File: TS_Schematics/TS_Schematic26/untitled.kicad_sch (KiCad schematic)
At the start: 28 parts, among them K2 IR(-) - TE Connectivity, K3 IR(+) - G2RL-1, K4 Precharge_G2RL-2, SW1 RL00801-500R, SW2 RL00801-500R, SW3 RL00801-500R, SW4 RL00801-500R, SW5 RL00801-500R, SW6 RL00801-500R, SW7 RL00801-500R, SW8 RL00801-500R, SW9 HV Master_Switch, U7 Precharge_G2R, U8 RML, U9 IMD

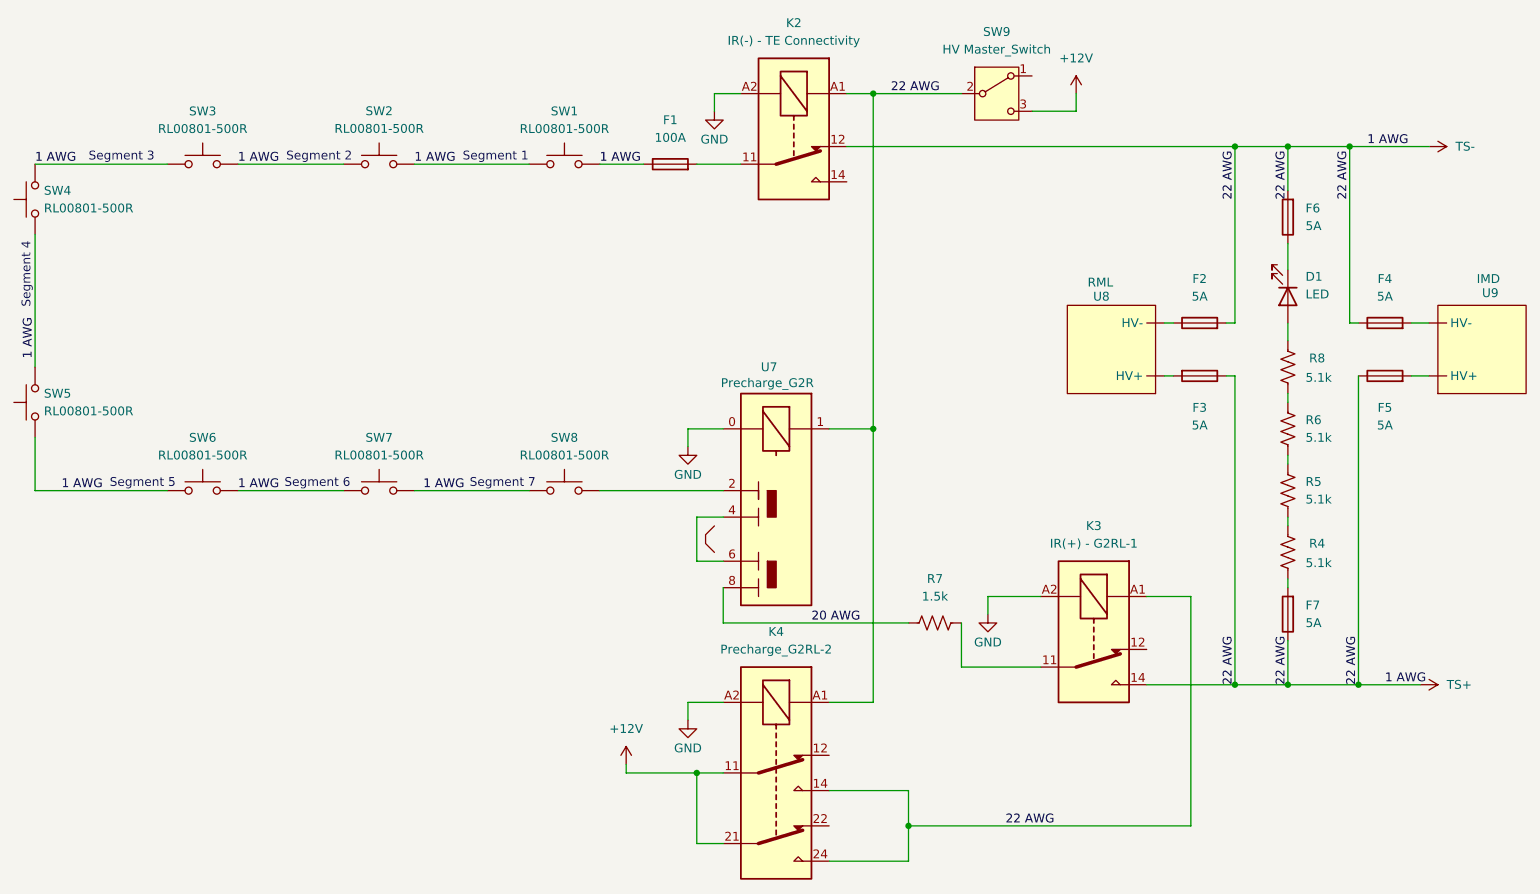
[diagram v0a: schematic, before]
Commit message: Charging FIxes
NMOS's Q1-4 had the wrong symbol as DGS, updated symbol and board with NMOS's Q1-4 to now have the correct symbol of GDS, to match the datasheet.
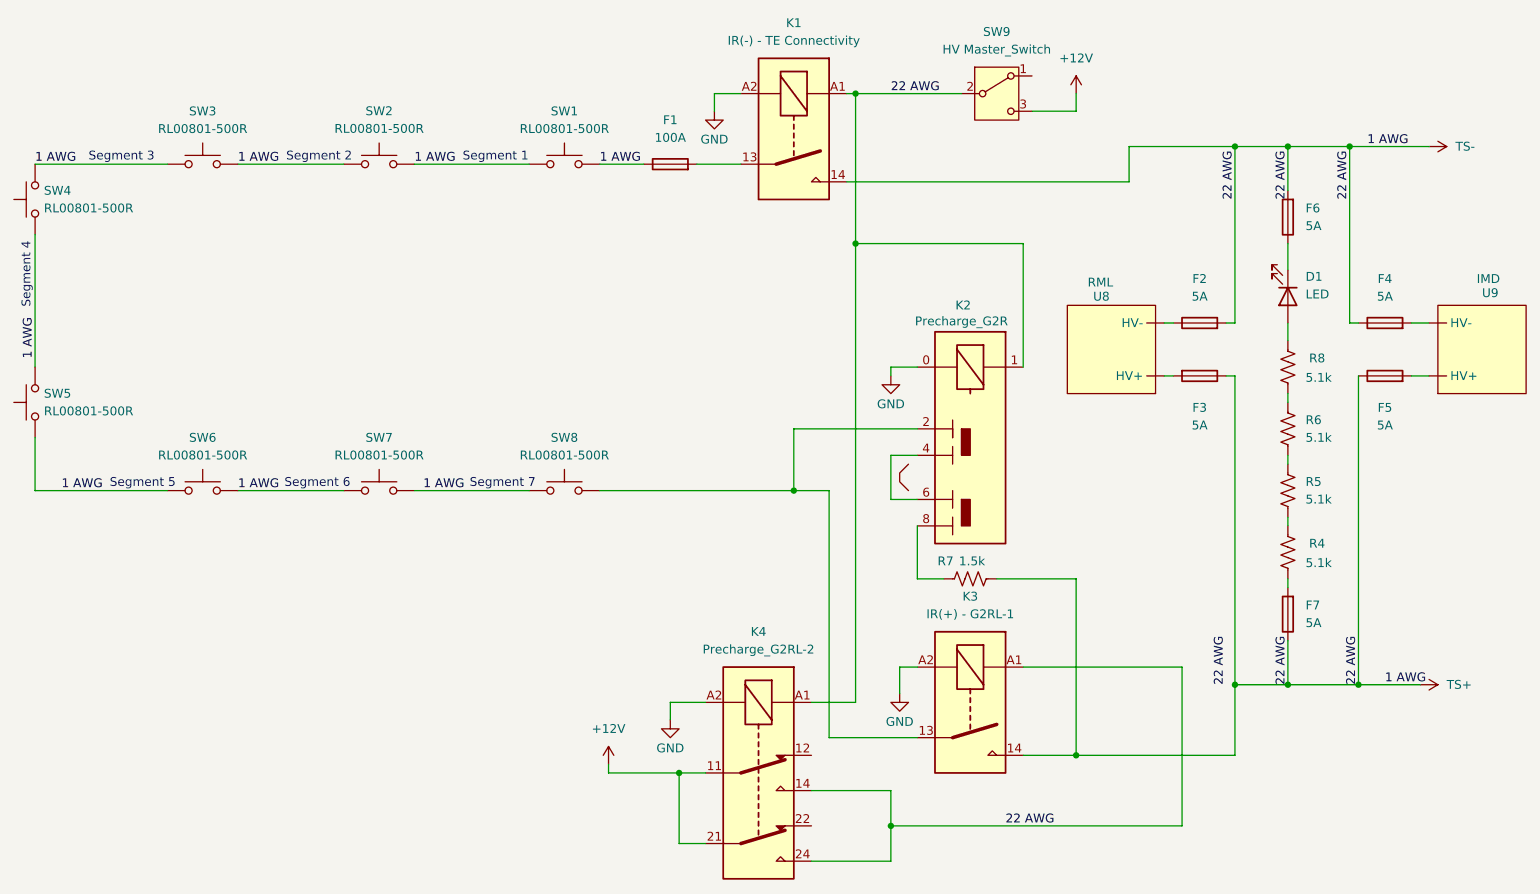
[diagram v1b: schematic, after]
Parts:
- removed K2: IR(-) - TE Connectivity, Relay_THT:Relay_SPDT_Omron_G2RL-1, symbol Relay:G2RL-1
- removed K3: IR(+) - G2RL-1, Relay_THT:Relay_SPDT_Omron_G2RL-1, symbol Relay:G2RL-1
- added K1: IR(-) - TE Connectivity, Relay_THT:Relay_SPST_Omron_G2RL-1A, symbol Relay:G2RL-1A
- added K3: IR(+) - G2RL-1, Relay_THT:Relay_SPST_Omron_G2RL-1A, symbol Relay:G2RL-1A
- renumbered U7 to K2
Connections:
- net GND: now also K1.A2, K3.A2
- net TS+: now also R7.1, K1.14, K1.A1, K3.14, K3.A1
- net at F1.2: now also K1.13
- net at K2.2, SW8.2: now also K3.13
- net 20 AWG: no longer names the net of K2.8, R7.2
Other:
- moved on the sheet: K2, K4, R7
